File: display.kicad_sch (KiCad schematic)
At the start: 72 parts, among them IC11 SN74LV1T125DBVR, IC18 TPD8S009DSMR, IC2 TPD8S009DSMR, IC6 PCA9517ADP, J1 HDMI_Micro-D_46756-1001, J2 DisplayPort_Mini_TE_2129320-3, M1 Jetson-Nano-new-release, T1 BSS138PW

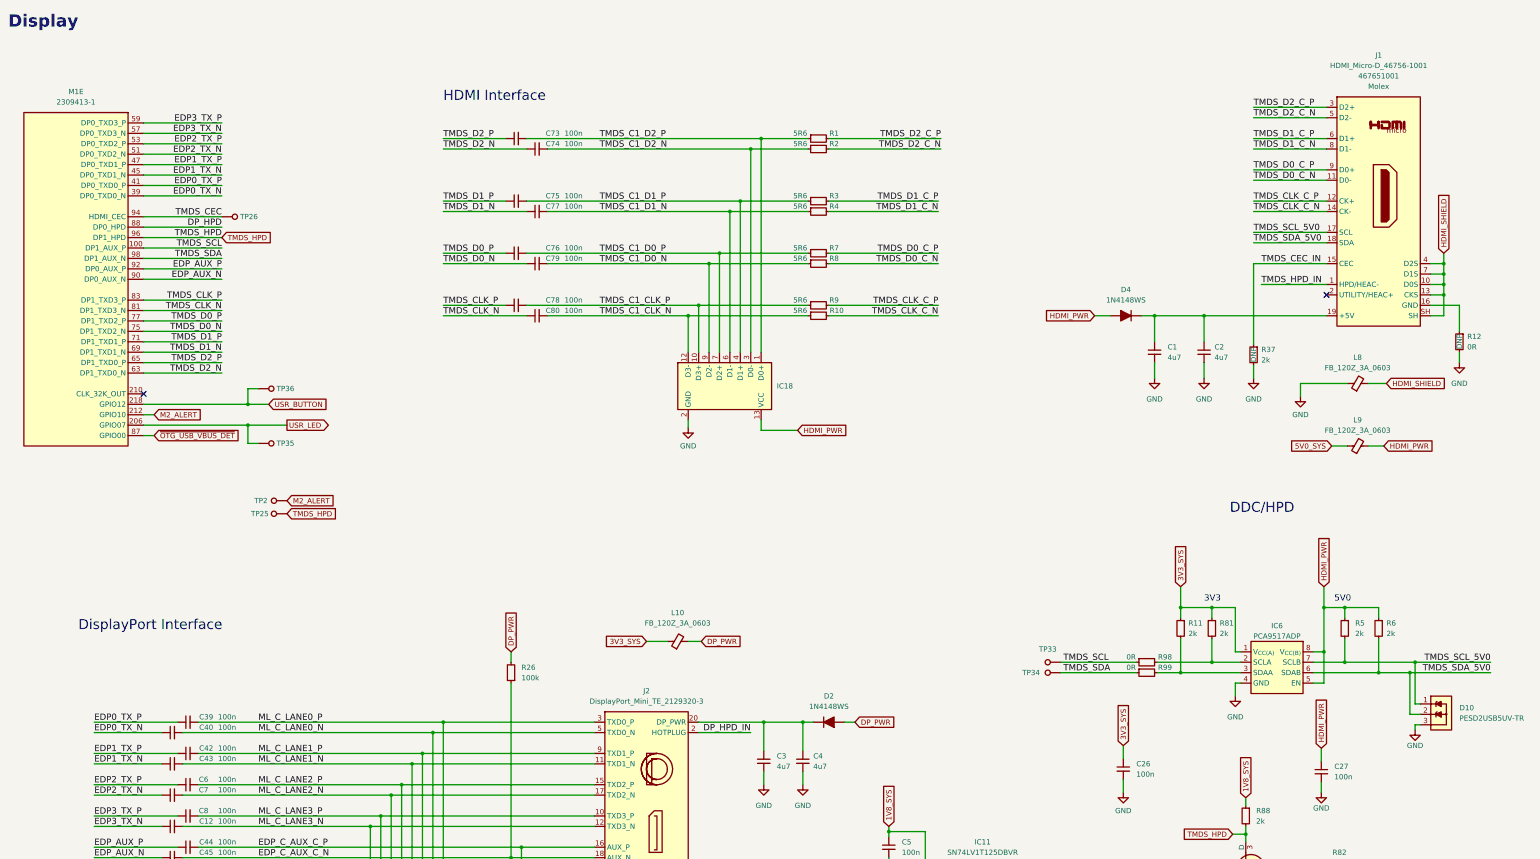
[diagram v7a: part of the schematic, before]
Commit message: [#56834] Fix components links
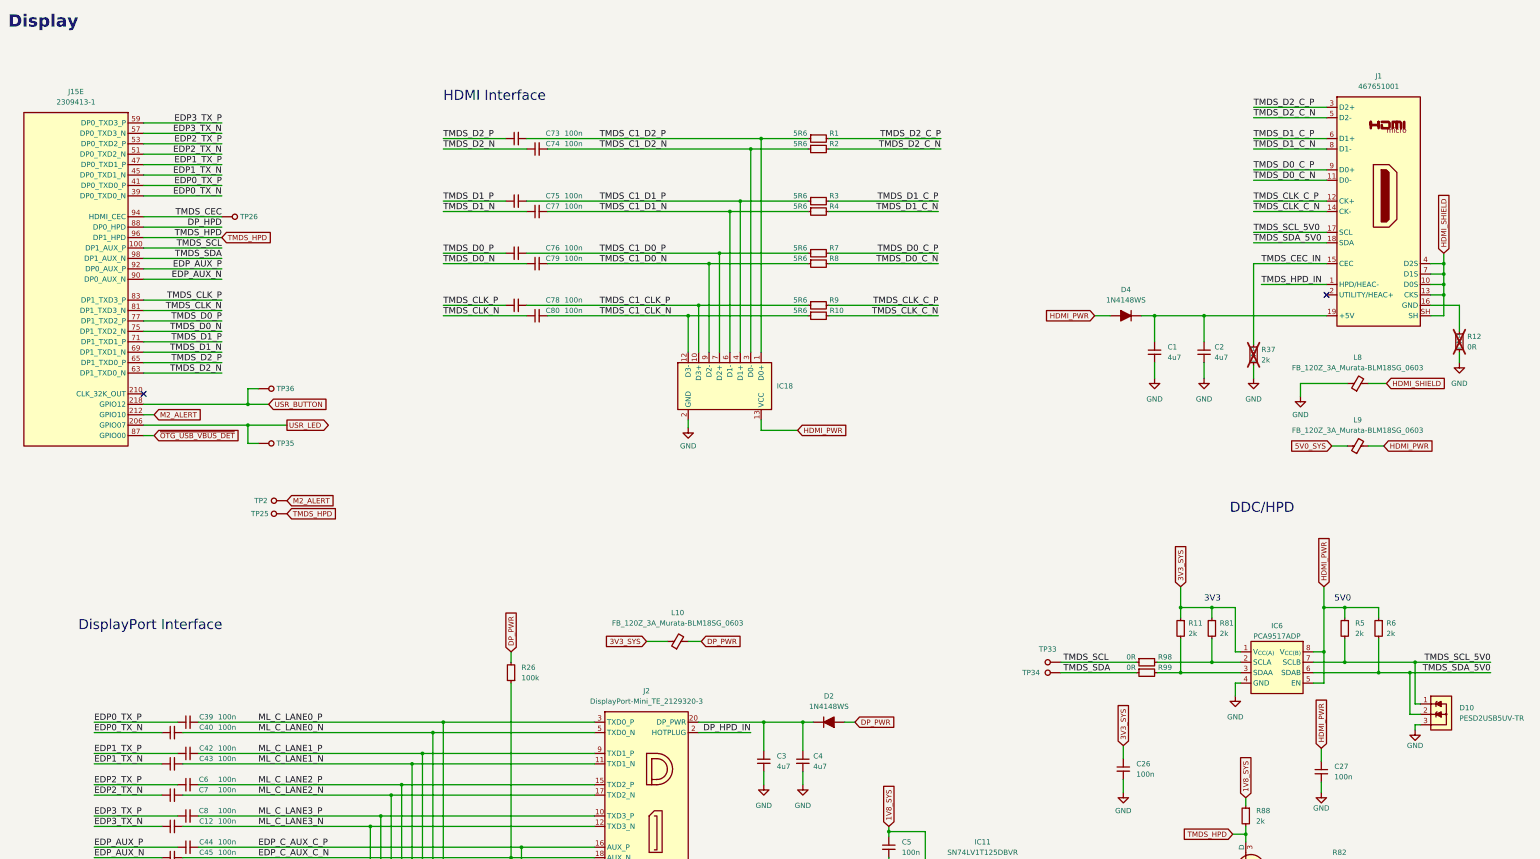
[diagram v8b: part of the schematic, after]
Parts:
- C1, C2, C3, C4: footprint antmicro-footprints:C_0402_1005Metric -> jetson-nano-baseboard-footprints:C_0402_1005Metric; symbol antmicroCapacitors0402:C_4u7_0402 -> jetson-nano-baseboard:C_4u7_0402
- C12, C26, C27, C39, C40, C42, C43, C44, C45, C5, C6, C7, C73, C74, C75, C76, C77, C78, C79, C8, C80: footprint antmicro-footprints:C_0402_1005Metric -> jetson-nano-baseboard-footprints:C_0402_1005Metric; symbol antmicroCapacitors0402:C_100n_0402 -> jetson-nano-baseboard:C_100n_0402
- D10, D11, D12: footprint antmicro-footprints:SOT-23-3 -> jetson-nano-baseboard-footprints:SOT-23-3; symbol antmicroTVSDiodes:PESD2USB5UV-TR -> jetson-nano-baseboard:PESD2USB5UV-TR; MPN PESD2USB5UV-TR -> PESD2USB5UV-TR
- D2, D4: footprint antmicro-footprints:D_SOD-323F -> jetson-nano-baseboard-footprints:D_SOD-323F; symbol antmicroDiodesRectifiersSingle:1N4148WS -> jetson-nano-baseboard:1N4148WS
- IC11: footprint antmicro-footprints:SOT-23-5 -> jetson-nano-baseboard-footprints:SOT-23-5; symbol antmicroLogicBuffersDriversReceiversTransceivers:SN74LV1T125DBVR -> jetson-nano-baseboard:SN74LV1T125DBVR
- IC18, IC2: footprint antmicro-footprints:R-PDSO-N15 -> jetson-nano-baseboard-footprints:R-PDSO-N15; symbol antmicroTVSDiodes:TPD8S009DSMR -> jetson-nano-baseboard:TPD8S009DSMR
- IC6: footprint antmicro-footprints:TSSOP-8_3x3mm_P0.65mm -> jetson-nano-baseboard-footprints:TSSOP-8_3x3mm_P0.65mm; symbol antmicroLogicTranslatorsLevelShifters:PCA9517ADP -> jetson-nano-baseboard:PCA9517ADP
- J1: value HDMI_Micro-D_46756-1001 -> HDMI-Micro-D_Molex_467561001; footprint antmicro-footprints:HDMI_Micro-D_Molex_46765-1x01 -> jetson-nano-baseboard-footprints:HDMI-Micro-D_Receptacle_Molex_467651001; symbol antmicroUSBDVIHDMIConnectors:HDMI_Micro-D_46756-1001 -> jetson-nano-baseboard:HDMI-Micro-D_Molex_467561001
- J15: renamed from M1; value Jetson-Nano-new-release -> Bus_DDR4_SODIMM_CUSTOM_Jetson-Nano-H9.2mm-socket; footprint antmicro-footprints:TE_2309413 -> jetson-nano-baseboard-footprints:TE_2309413; symbol antmicroSoMConnectors:Jetson-Nano-new-release -> jetson-nano-baseboard:Bus_DDR4_SODIMM_CUSTOM_Jetson-Nano-H9.2mm-socket
- J2: value DisplayPort_Mini_TE_2129320-3 -> DisplayPort-Mini_TE_2129320-3; footprint antmicro-footprints:DisplayPort_Mini_TE_2129320-3 -> jetson-nano-baseboard-footprints:DisplayPort-Mini_Receptacle_TE_2129320-3; symbol antmicroUSBDVIHDMIConnectors:DisplayPort_Mini_TE_2129320-3 -> jetson-nano-baseboard:DisplayPort-Mini_TE_2129320-3
- L10, L8, L9: value FB_120Z_3A_0603 -> FB_120Z_3A_Murata-BLM18SG_0603; footprint antmicro-footprints:FB_0603_1608Metric -> jetson-nano-baseboard-footprints:FB_0603_1608Metric; symbol antmicroFerriteBeadsandChips:FB_120Z_3A_0603 -> jetson-nano-baseboard:FB_120Z_3A_Murata-BLM18SG_0603
- R1, R10, R2, R3, R4, R7, R8, R9: footprint antmicro-footprints:R_0402_1005Metric -> jetson-nano-baseboard-footprints:R_0402_1005Metric; symbol antmicroResistors0402:R_5R6_0402 -> jetson-nano-baseboard:R_5R6_0402
- R100, R26, R30: footprint antmicro-footprints:R_0402_1005Metric -> jetson-nano-baseboard-footprints:R_0402_1005Metric; symbol antmicroResistors0402:R_100k_0402 -> jetson-nano-baseboard:R_100k_0402
- R11, R5, R6, R81, R83, R88: footprint antmicro-footprints:R_0402_1005Metric -> jetson-nano-baseboard-footprints:R_0402_1005Metric; symbol antmicroResistors0402:R_2k_0402 -> jetson-nano-baseboard:R_2k_0402
- R12: footprint antmicro-footprints:R_0402_1005Metric -> jetson-nano-baseboard-footprints:R_0402_1005Metric; symbol antmicroResistors0402:R_0R_0402 -> jetson-nano-baseboard:R_0R_0402; now not fitted; now left out of the parts list
- R31, R32: footprint antmicro-footprints:R_0402_1005Metric -> jetson-nano-baseboard-footprints:R_0402_1005Metric; symbol antmicroResistors0402:R_1M_0402 -> jetson-nano-baseboard:R_1M_0402
- R37: footprint antmicro-footprints:R_0402_1005Metric -> jetson-nano-baseboard-footprints:R_0402_1005Metric; symbol antmicroResistors0402:R_2k_0402 -> jetson-nano-baseboard:R_2k_0402; now not fitted; now left out of the parts list
- R82, R98, R99: footprint antmicro-footprints:R_0402_1005Metric -> jetson-nano-baseboard-footprints:R_0402_1005Metric; symbol antmicroResistors0402:R_0R_0402 -> jetson-nano-baseboard:R_0R_0402
- T1: footprint antmicro-footprints:SC70-3 -> jetson-nano-baseboard-footprints:SC70-3; symbol antmicroTransistorsFETsMOSFETsSingle:BSS138PW -> jetson-nano-baseboard:BSS138PW
- TP2, TP25, TP26, TP33, TP34, TP35, TP36: footprint antmicro-footprints:TP_SMD_1.5mm -> jetson-nano-baseboard-footprints:TP_SMD_1.5mm; symbol antmicroTestPoints:TP_1.5mm_SMD -> jetson-nano-baseboard:TP_1.5mm_SMD; MPN N/A -> (none); Manufacturer N/A -> (none)
